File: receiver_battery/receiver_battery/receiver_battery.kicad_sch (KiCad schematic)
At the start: 36 parts, among them U1 NRF24L01_Breakout

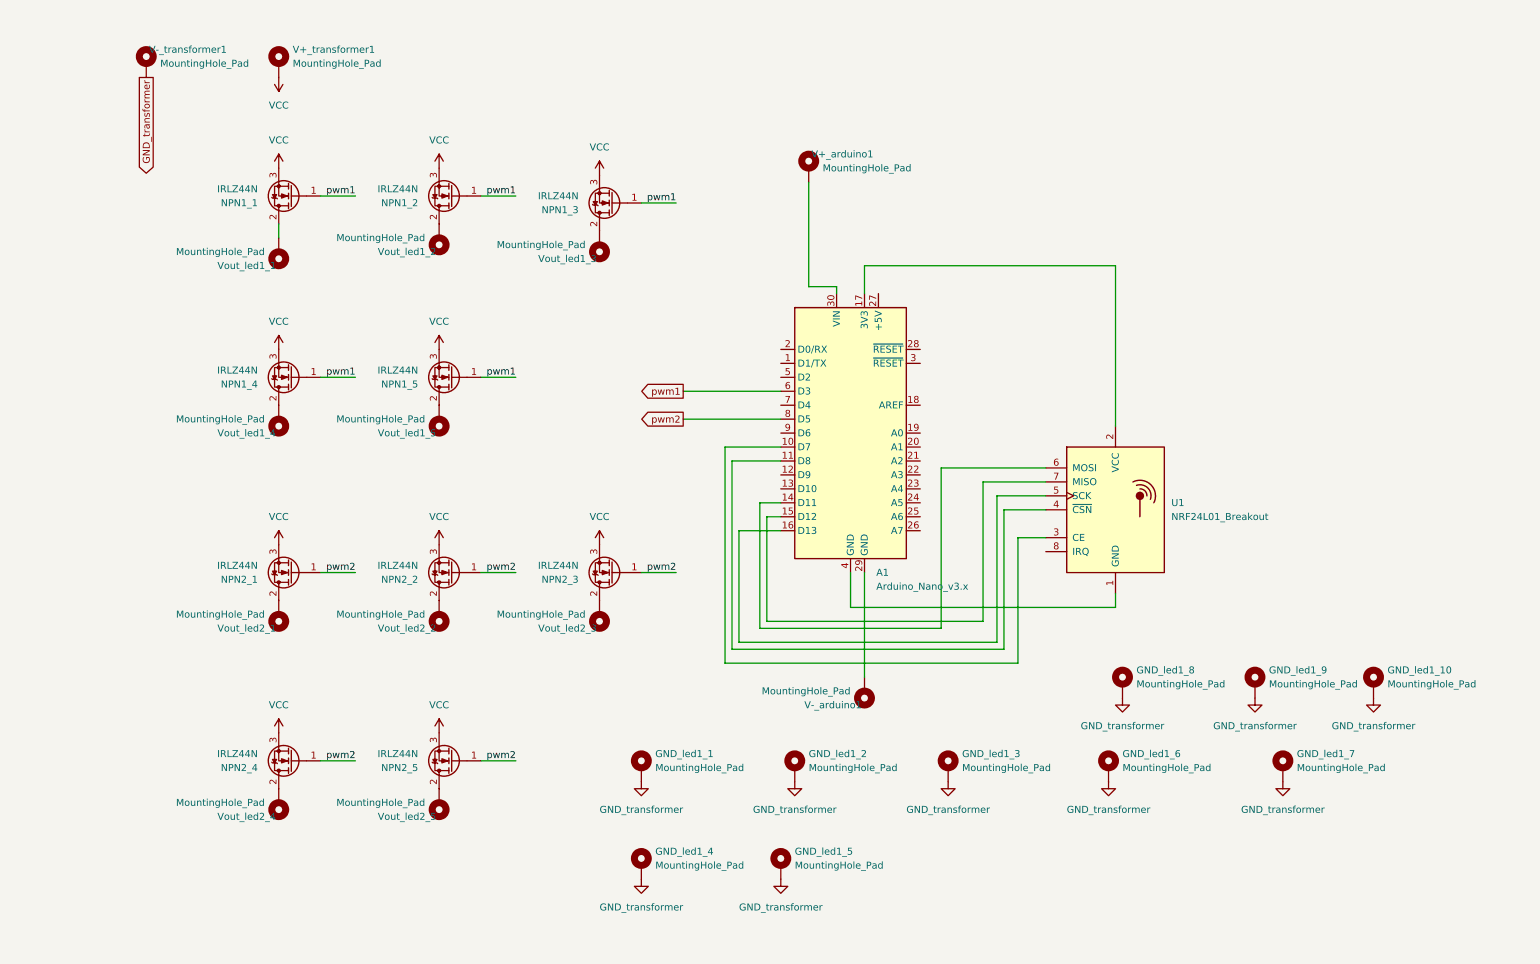
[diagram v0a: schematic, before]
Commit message: pulldown on each transistor
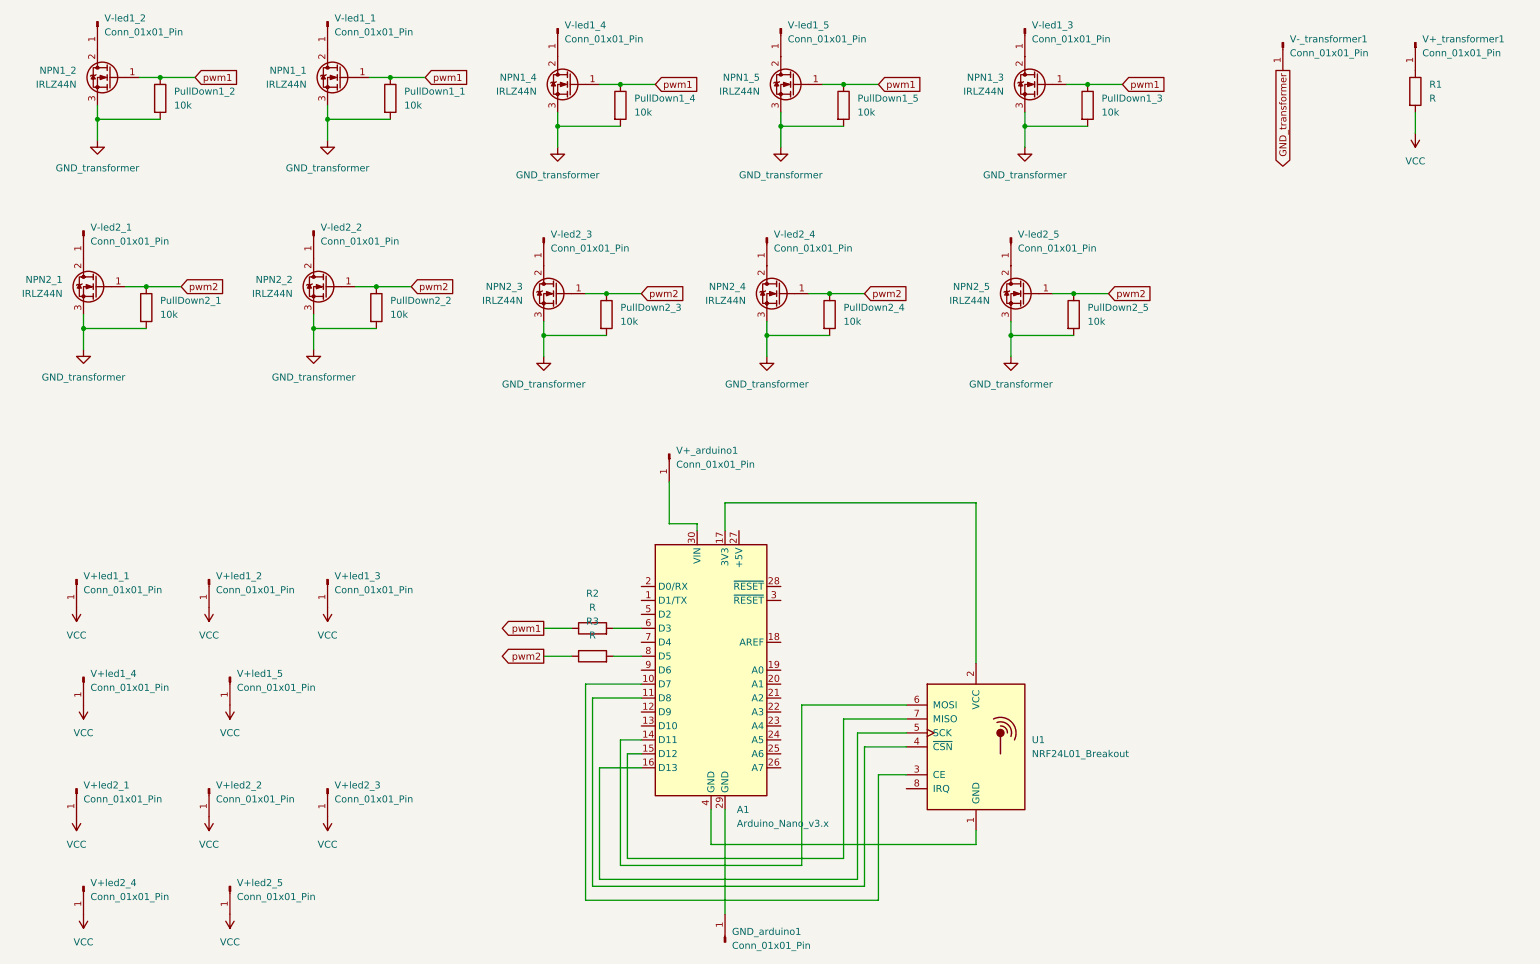
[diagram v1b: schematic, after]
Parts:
- removed GND_led1_1, GND_led1_10, GND_led1_2, GND_led1_3, GND_led1_4, GND_led1_5, GND_led1_6, GND_led1_7, GND_led1_8, GND_led1_9, V+_arduino1, V+_transformer1, V-_arduino1, V-_transformer1, Vout_led1_1, Vout_led1_2, Vout_led1_3, Vout_led1_4, Vout_led1_5, Vout_led2_1, Vout_led2_2, Vout_led2_3, Vout_led2_4, Vout_led2_5: MountingHole_Pad, MountingHole:MountingHole_2.5mm_Pad_TopBottom, symbol Mechanical:MountingHole_Pad
- added GND_arduino1, V+_arduino1, V+_transformer1, V+led1_1, V+led1_2, V+led1_3, V+led1_4, V+led1_5, V+led2_1, V+led2_2, V+led2_3, V+led2_4, V+led2_5, V-_transformer1, V-led1_1, V-led1_2, V-led1_3, V-led1_4, V-led1_5, V-led2_1, V-led2_2, V-led2_3, V-led2_4, V-led2_5: Conn_01x01_Pin, Connector_Wire:SolderWire-1.5sqmm_1x01_D1.7mm_OD3.9mm, symbol Connector:Conn_01x01_Pin
- added PullDown1_1, PullDown1_2, PullDown1_3, PullDown1_4, PullDown1_5, PullDown2_1, PullDown2_2, PullDown2_3, PullDown2_4, PullDown2_5: 10k, Resistor_THT:R_Axial_DIN0207_L6.3mm_D2.5mm_P7.62mm_Horizontal, symbol Device:R
- added R1, R2, R3: R, Resistor_THT:R_Axial_DIN0207_L6.3mm_D2.5mm_P7.62mm_Horizontal, symbol Device:R
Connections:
- net GND_transformer: now also NPN1_1.3 (S), NPN1_2.3 (S), NPN1_3.3 (S), NPN1_4.3 (S), NPN1_5.3 (S), NPN2_1.3 (S), NPN2_2.3 (S), NPN2_3.3 (S), NPN2_4.3 (S), NPN2_5.3 (S), PullDown1_1.2, PullDown1_2.2, PullDown1_3.2, PullDown1_4.2, PullDown1_5.2, PullDown2_1.2, PullDown2_2.2, PullDown2_3.2, PullDown2_4.2, PullDown2_5.2, V-_transformer1.1 (Pin_1)
- net VCC: now also R1.2, V+led1_1.1 (Pin_1), V+led1_2.1 (Pin_1), V+led1_3.1 (Pin_1), V+led1_4.1 (Pin_1), V+led1_5.1 (Pin_1), V+led2_1.1 (Pin_1), V+led2_2.1 (Pin_1), V+led2_3.1 (Pin_1), V+led2_4.1 (Pin_1), V+led2_5.1 (Pin_1); no longer NPN1_1.3 (S), NPN1_2.3 (S), NPN1_3.3 (S), NPN1_4.3 (S), NPN1_5.3 (S), NPN2_1.3 (S), NPN2_2.3 (S), NPN2_3.3 (S), NPN2_4.3 (S), NPN2_5.3 (S)
- net pwm1: now also PullDown1_1.1, PullDown1_2.1, PullDown1_3.1, PullDown1_4.1, PullDown1_5.1, R2.1; no longer A1.6 (D3)
- net pwm2: now also PullDown2_1.1, PullDown2_2.1, PullDown2_3.1, PullDown2_4.1, PullDown2_5.1, R3.1; no longer A1.8 (D5)
- net at NPN1_3.2 (D): now also V-led1_3.1 (Pin_1)
- net at NPN2_5.2 (D): now also V-led2_5.1 (Pin_1)
- net at NPN2_1.2 (D): now also V-led2_1.1 (Pin_1)
- net at NPN1_4.2 (D): now also V-led1_4.1 (Pin_1)
- net at NPN1_5.2 (D): now also V-led1_5.1 (Pin_1)
- net at NPN2_3.2 (D): now also V-led2_3.1 (Pin_1)
- net at NPN2_2.2 (D): now also V-led2_2.1 (Pin_1)
- net at NPN1_2.2 (D): now also V-led1_2.1 (Pin_1)
- net at NPN2_4.2 (D): now also V-led2_4.1 (Pin_1)
- net at NPN1_1.2 (D): now also V-led1_1.1 (Pin_1)
- net at A1.29 (GND): now also GND_arduino1.1 (Pin_1)
- net at A1.30 (VIN): now also V+_arduino1.1 (Pin_1)
- new net: R1.1, V+_transformer1.1 (Pin_1)
- new net: A1.8 (D5), R3.2
- new net: A1.6 (D3), R2.2
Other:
- moved on the sheet: A1, U1

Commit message: only 2 pull down res + res for each led
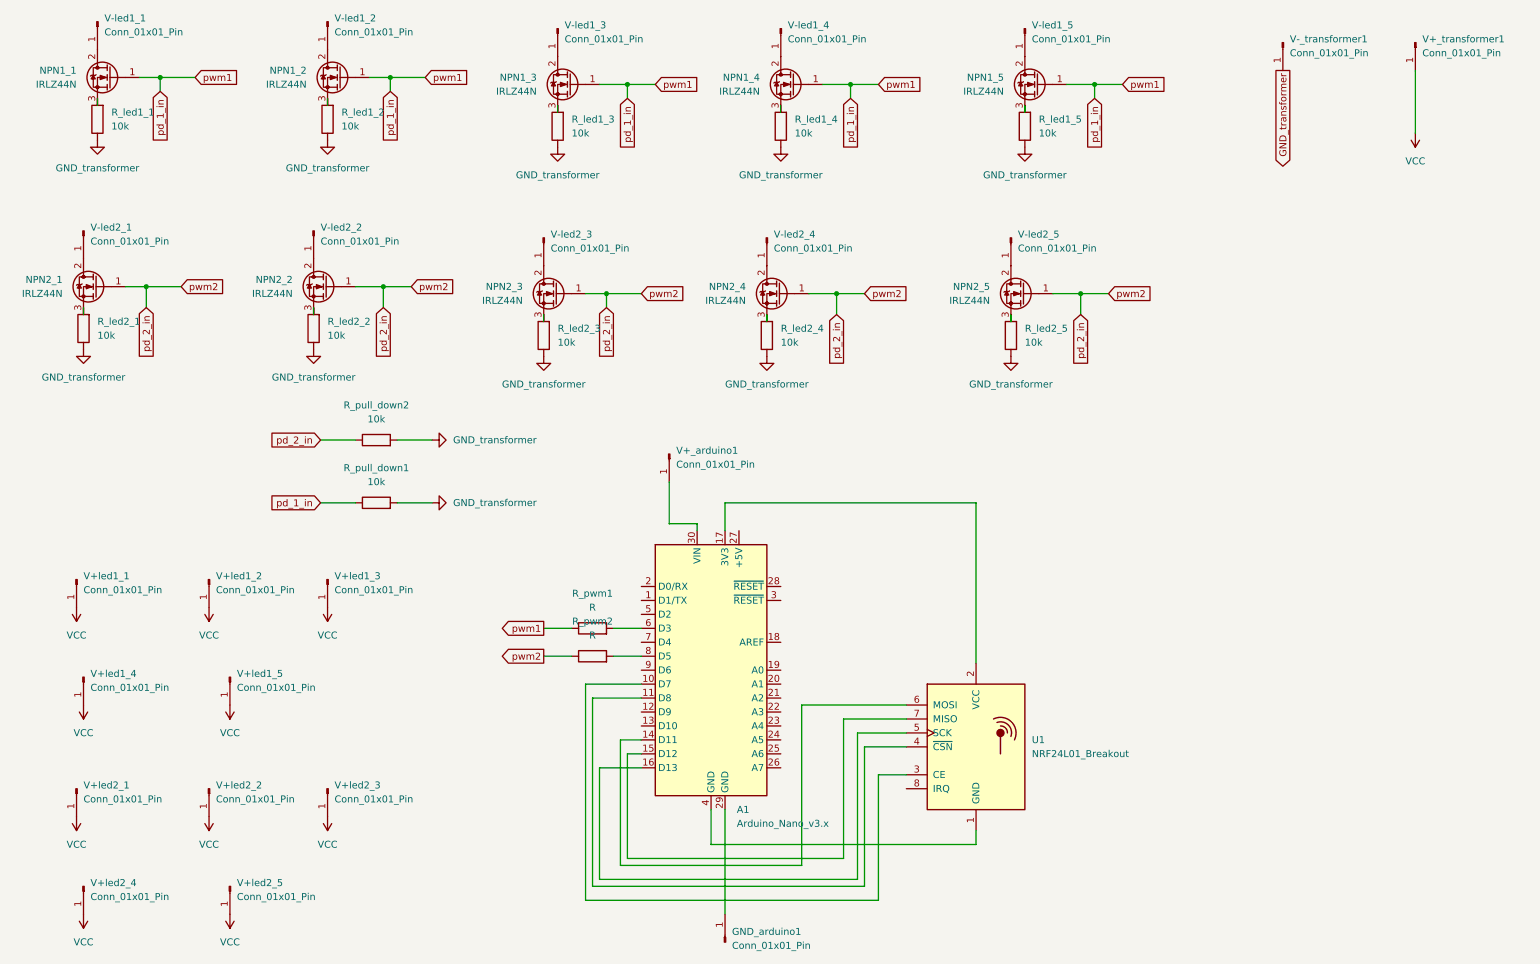
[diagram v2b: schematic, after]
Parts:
- removed PullDown1_1, PullDown1_2, PullDown1_3, PullDown1_4, PullDown1_5, PullDown2_1, PullDown2_2, PullDown2_3, PullDown2_4, PullDown2_5: 10k, Resistor_THT:R_Axial_DIN0207_L6.3mm_D2.5mm_P7.62mm_Horizontal, symbol Device:R
- removed R1: R, Resistor_THT:R_Axial_DIN0207_L6.3mm_D2.5mm_P7.62mm_Horizontal, symbol Device:R
- added R_led1_1, R_led1_2, R_led1_3, R_led1_4, R_led1_5, R_led2_1, R_led2_2, R_led2_3, R_led2_4, R_led2_5, R_pull_down1, R_pull_down2: 10k, Resistor_THT:R_Axial_DIN0207_L6.3mm_D2.5mm_P7.62mm_Horizontal, symbol Device:R
- renumbered NPN1_2 to NPN1_1, NPN1_1 to NPN1_2, NPN1_4 to NPN1_3, NPN1_5 to NPN1_4, NPN1_3 to NPN1_5, R2 to R_pwm1, R3 to R_pwm2, V-led1_2 to V-led1_1, V-led1_1 to V-led1_2, V-led1_4 to V-led1_3, V-led1_5 to V-led1_4, V-led1_3 to V-led1_5
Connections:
- net GND_transformer: now also R_led1_1.1, R_led1_2.1, R_led1_3.1, R_led1_4.1, R_led1_5.1, R_led2_1.1, R_led2_2.1, R_led2_3.1, R_led2_4.1, R_led2_5.1, R_pull_down1.2, R_pull_down2.2; no longer NPN1_1.3 (S), NPN1_2.3 (S), NPN1_3.3 (S), NPN1_4.3 (S), NPN1_5.3 (S), NPN2_1.3 (S), NPN2_2.3 (S), NPN2_3.3 (S), NPN2_4.3 (S), NPN2_5.3 (S)
- net VCC: now also V+_transformer1.1 (Pin_1)
- net pwm1 renamed pd_1_in
- net pd_1_in: now also R_pull_down1.1
- net pwm2 renamed pd_2_in
- net pd_2_in: now also R_pull_down2.1
- new net: NPN1_4.3 (S), R_led1_4.2
- new net: NPN1_1.3 (S), R_led1_1.2
- new net: NPN2_1.3 (S), R_led2_1.2
- new net: NPN1_5.3 (S), R_led1_5.2
- new net: NPN2_2.3 (S), R_led2_2.2
- new net: NPN1_3.3 (S), R_led1_3.2
- new net: NPN2_5.3 (S), R_led2_5.2
- new net: NPN1_2.3 (S), R_led1_2.2
- new net: NPN2_3.3 (S), R_led2_3.2
- new net: NPN2_4.3 (S), R_led2_4.2

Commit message: large cock resistor
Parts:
- R_led1_1, R_led1_2, R_led1_3, R_led1_4, R_led1_5, R_led2_1, R_led2_2, R_led2_3, R_led2_4, R_led2_5: footprint Resistor_THT:R_Axial_DIN0207_L6.3mm_D2.5mm_P7.62mm_Horizontal -> Resistor_THT:R_Axial_Power_L20.0mm_W6.4mm_P7.62mm_Vertical
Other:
- moved on the sheet: R_pull_down1, R_pull_down2, V+_transformer1
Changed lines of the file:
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@@
 	(wire
 		(pts
-			(xy 83.82 95.25) (xy 90.17 95.25)
+			(xy 85.09 99.06) (xy 91.44 99.06)
 		)
 		(stroke
@@
 	(wire
 		(pts
-			(xy 269.24 27.94) (xy 269.24 39.37)
+			(xy 266.7 27.94) (xy 266.7 39.37)
 		)
 		(stroke
@@
 	(wire
 		(pts
-			(xy 69.85 95.25) (xy 76.2 95.25)
+			(xy 71.12 99.06) (xy 77.47 99.06)
 		)
 		(stroke
@@
 	(wire
 		(pts
-			(xy 83.82 106.68) (xy 90.17 106.68)
+			(xy 85.09 110.49) (xy 91.44 110.49)
 		)
 		(stroke
@@
 	(wire
 		(pts
-			(xy 69.85 106.68) (xy 76.2 106.68)
+			(xy 71.12 110.49) (xy 77.47 110.49)
 		)
 		(stroke
@@
 		)
 		(stroke
-			(width 0)
+			(width 0.0254)
 			(type default)
 		)
@@
 	(global_label "pd_2_in"
 		(shape input)
-		(at 69.85 95.25 180)
+		(at 71.12 99.06 180)
 		(fields_autoplaced yes)
 		(effects
@@
 		)
 		(property "Intersheetrefs" "${INTERSHEET_REFS}"
-			(at 59.6683 95.25 0)
+			(at 60.9383 99.06 0)
 			(effects
 				(font
@@
 	(global_label "pd_1_in"
 		(shape input)
-		(at 69.85 106.68 180)
+		(at 71.12 110.49 180)
 		(fields_autoplaced yes)
 		(effects
@@
 		)
 		(property "Intersheetrefs" "${INTERSHEET_REFS}"
-			(at 59.6683 106.68 0)
+			(at 60.9383 110.49 0)
 			(effects
 				(font
@@
 	(symbol
 		(lib_id "Connector:Conn_01x01_Pin")
-		(at 269.24 22.86 270)
+		(at 266.7 22.86 270)
 		(unit 1)
 		(exclude_from_sim no)
@@
 		(fields_autoplaced yes)
 		(property "Reference" "V+_transformer1"
-			(at 270.51 22.2249 90)
+			(at 267.97 22.2249 90)
 			(effects
 				(font
@@
 		)
 		(property "Value" "Conn_01x01_Pin"
-			(at 270.51 24.7649 90)
+			(at 267.97 24.7649 90)
 			(effects
 				(font
@@
 		)
 		(property "Footprint" "Connector_Wire:SolderWire-1.5sqmm_1x01_D1.7mm_OD3.9mm"
-			(at 269.24 22.86 0)
+			(at 266.7 22.86 0)
 			(effects
 				(font
@@
 		)
 		(property "Datasheet" "~"
-			(at 269.24 22.86 0)
+			(at 266.7 22.86 0)
 			(effects
 				(font
@@
 		)
 		(property "Description" ""
-			(at 269.24 22.86 0)
+			(at 266.7 22.86 0)
 			(effects
 				(font
@@
 		(on_board yes)
 		(dnp no)
-		(fields_autoplaced yes)
 		(property "Reference" "R_pwm2"
-			(at 119.38 128.27 90)
+			(at 118.872 137.414 90)
 			(effects
 				(font
@@
 		)
 		(property "Value" "R"
-			(at 119.38 130.81 90)
+			(at 119.634 139.7 90)
 			(effects
 				(font
@@
 			)
 		)
-		(property "Footprint" "Resistor_THT:R_Axial_DIN0207_L6.3mm_D2.5mm_P7.62mm_Horizontal"
+		(property "Footprint" "Resistor_THT:R_Axial_Power_L20.0mm_W6.4mm_P7.62mm_Vertical"
 			(at 70.358 74.93 90)
 			(effects
@@
 	(symbol
 		(lib_id "Device:R")
-		(at 80.01 95.25 90)
+		(at 81.28 99.06 90)
 		(unit 1)
 		(exclude_from_sim no)
@@
 		(fields_autoplaced yes)
 		(property "Reference" "R_pull_down2"
-			(at 80.01 88.9 90)
+			(at 81.28 92.71 90)
 			(effects
 				(font
@@
 		)
 		(property "Value" "10k"
-			(at 80.01 91.44 90)
+			(at 81.28 95.25 90)
 			(effects
 				(font
@@
 		)
 		(property "Footprint" "Resistor_THT:R_Axial_DIN0207_L6.3mm_D2.5mm_P7.62mm_Horizontal"
-			(at 80.01 97.028 90)
+			(at 81.28 100.838 90)
 			(effects
 				(font
@@
 		)
 		(property "Datasheet" "~"
-			(at 80.01 95.25 0)
+			(at 81.28 99.06 0)
 			(effects
 				(font
@@
 		)
 		(property "Description" "Resistor"
-			(at 80.01 95.25 0)
+			(at 81.28 99.06 0)
 			(effects
 				(font
@@
 			)
 		)
-		(property "Footprint" "Resistor_THT:R_Axial_DIN0207_L6.3mm_D2.5mm_P7.62mm_Horizontal"
+		(property "Footprint" "Resistor_THT:R_Axial_Power_L20.0mm_W6.4mm_P7.62mm_Vertical"
 			(at 28.448 74.93 90)
 			(effects
@@
 	(symbol
 		(lib_id "Device:R")
-		(at 80.01 106.68 90)
+		(at 81.28 110.49 90)
 		(unit 1)
 		(exclude_from_sim no)
@@
 		(fields_autoplaced yes)
 		(property "Reference" "R_pull_down1"
-			(at 80.01 100.33 90)
+			(at 81.28 104.14 90)
 			(effects
 				(font
@@
 		)
 		(property "Value" "10k"
-			(at 80.01 102.87 90)
+			(at 81.28 106.68 90)
 			(effects
 				(font
@@
 		)
 		(property "Footprint" "Resistor_THT:R_Axial_DIN0207_L6.3mm_D2.5mm_P7.62mm_Horizontal"
-			(at 80.01 108.458 90)
+			(at 81.28 112.268 90)
 			(effects
 				(font
@@
 		)
 		(property "Datasheet" "~"
-			(at 80.01 106.68 0)
+			(at 81.28 110.49 0)
 			(effects
 				(font
@@
 		)
 		(property "Description" "Resistor"
-			(at 80.01 106.68 0)
+			(at 81.28 110.49 0)
 			(effects
 				(font
@@
 	(symbol
 		(lib_id "power:VCC")
-		(at 269.24 39.37 180)
+		(at 266.7 39.37 180)
 		(unit 1)
 		(exclude_from_sim no)
@@
 		(fields_autoplaced yes)
 		(property "Reference" "#PWR011"
-			(at 269.24 35.56 0)
+			(at 266.7 35.56 0)
 			(effects
 				(font
@@
 		)
 		(property "Value" "VCC"
-			(at 269.24 44.45 0)
+			(at 266.7 44.45 0)
 			(effects
 				(font
@@
 		)
 		(property "Footprint" ""
-			(at 269.24 39.37 0)
+			(at 266.7 39.37 0)
 			(effects
 				(font
@@
 		)
 		(property "Datasheet" ""
-			(at 269.24 39.37 0)
+			(at 266.7 39.37 0)
 			(effects
 				(font
@@
 		)
 		(property "Description" "Power symbol creates a global label with name \"VCC\""
-			(at 269.24 39.37 0)
+			(at 266.7 39.37 0)
 			(effects
 				(font
@@
 			)
 		)
-		(property "Footprint" "Resistor_THT:R_Axial_DIN0207_L6.3mm_D2.5mm_P7.62mm_Horizontal"
+		(property "Footprint" "Resistor_THT:R_Axial_Power_L20.0mm_W6.4mm_P7.62mm_Vertical"
 			(at 197.358 76.2 90)
 			(effects
@@
 			)
 		)
-		(property "Footprint" "Resistor_THT:R_Axial_DIN0207_L6.3mm_D2.5mm_P7.62mm_Horizontal"
+		(property "Footprint" "Resistor_THT:R_Axial_Power_L20.0mm_W6.4mm_P7.62mm_Vertical"
 			(at 30.988 36.83 90)
 			(effects
@@
 			)
 		)
-		(property "Footprint" "Resistor_THT:R_Axial_DIN0207_L6.3mm_D2.5mm_P7.62mm_Horizontal"
+		(property "Footprint" "Resistor_THT:R_Axial_Power_L20.0mm_W6.4mm_P7.62mm_Vertical"
 			(at 72.898 36.83 90)
 			(effects
@@
 			)
 		)
-		(property "Footprint" "Resistor_THT:R_Axial_DIN0207_L6.3mm_D2.5mm_P7.62mm_Horizontal"
+		(property "Footprint" "Resistor_THT:R_Axial_Power_L20.0mm_W6.4mm_P7.62mm_Vertical"
 			(at 112.268 76.2 90)
 			(effects
@@
 			)
 		)
-		(property "Footprint" "Resistor_THT:R_Axial_DIN0207_L6.3mm_D2.5mm_P7.62mm_Horizontal"
+		(property "Footprint" "Resistor_THT:R_Axial_Power_L20.0mm_W6.4mm_P7.62mm_Vertical"
 			(at 152.908 76.2 90)
 			(effects
@@
 			)
 		)
-		(property "Footprint" "Resistor_THT:R_Axial_DIN0207_L6.3mm_D2.5mm_P7.62mm_Horizontal"
+		(property "Footprint" "Resistor_THT:R_Axial_Power_L20.0mm_W6.4mm_P7.62mm_Vertical"
 			(at 114.808 38.1 90)
 			(effects
@@
 	(symbol
 		(lib_id "power:GND")
-		(at 90.17 106.68 90)
+		(at 91.44 110.49 90)
 		(unit 1)
 		(exclude_from_sim no)
@@
 		(fields_autoplaced yes)
 		(property "Reference" "#PWR033"
-			(at 96.52 106.68 0)
+			(at 97.79 110.49 0)
 			(effects
 				(font
@@
 		)
 		(property "Value" "GND_transformer"
-			(at 93.98 106.6799 90)
+			(at 95.25 110.4899 90)
 			(effects
 				(font
@@
 		)
 		(property "Footprint" ""
-			(at 90.17 106.68 0)
+			(at 91.44 110.49 0)
 			(effects
 				(font
@@
 		)
 		(property "Datasheet" ""
-			(at 90.17 106.68 0)
+			(at 91.44 110.49 0)
 			(effects
 				(font
@@
 		)
 		(property "Description" "Power symbol creates a global label with name \"GND\" , ground"
-			(at 90.17 106.68 0)
+			(at 91.44 110.49 0)
 			(effects
 				(font
@@
 			)
 		)
-		(property "Footprint" "Resistor_THT:R_Axial_DIN0207_L6.3mm_D2.5mm_P7.62mm_Horizontal"
+		(property "Footprint" "Resistor_THT:R_Axial_Power_L20.0mm_W6.4mm_P7.62mm_Vertical"
 			(at 199.898 38.1 90)
 			(effects
@@
 			)
 		)
-		(property "Footprint" "Resistor_THT:R_Axial_DIN0207_L6.3mm_D2.5mm_P7.62mm_Horizontal"
+		(property "Footprint" "Resistor_THT:R_Axial_Power_L20.0mm_W6.4mm_P7.62mm_Vertical"
 			(at 155.448 38.1 90)
 			(effects
@@
 	(symbol
 		(lib_id "power:GND")
-		(at 90.17 95.25 90)
+		(at 91.44 99.06 90)
 		(unit 1)
 		(exclude_from_sim no)
@@
 		(fields_autoplaced yes)
 		(property "Reference" "#PWR032"
-			(at 96.52 95.25 0)
+			(at 97.79 99.06 0)
 			(effects
 				(font
@@
 		)
 		(property "Value" "GND_transformer"
-			(at 93.98 95.2499 90)
+			(at 95.25 99.0599 90)
 			(effects
 				(font
@@
 		)
 		(property "Footprint" ""
-			(at 90.17 95.25 0)
+			(at 91.44 99.06 0)
 			(effects
 				(font
@@
 		)
 		(property "Datasheet" ""
-			(at 90.17 95.25 0)
+			(at 91.44 99.06 0)
 			(effects
 				(font
@@
 		)
 		(property "Description" "Power symbol creates a global label with name \"GND\" , ground"
-			(at 90.17 95.25 0)
+			(at 91.44 99.06 0)
 			(effects
 				(font
